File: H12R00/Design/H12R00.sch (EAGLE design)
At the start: 35 parts, among them P1 HEXABIT_17.32_NO_P3_P6, U1 STM32F091CBU6, U2 AD628ARZ, U3 REF193GSZ, X1 XTALL_CSTCE8M00G52

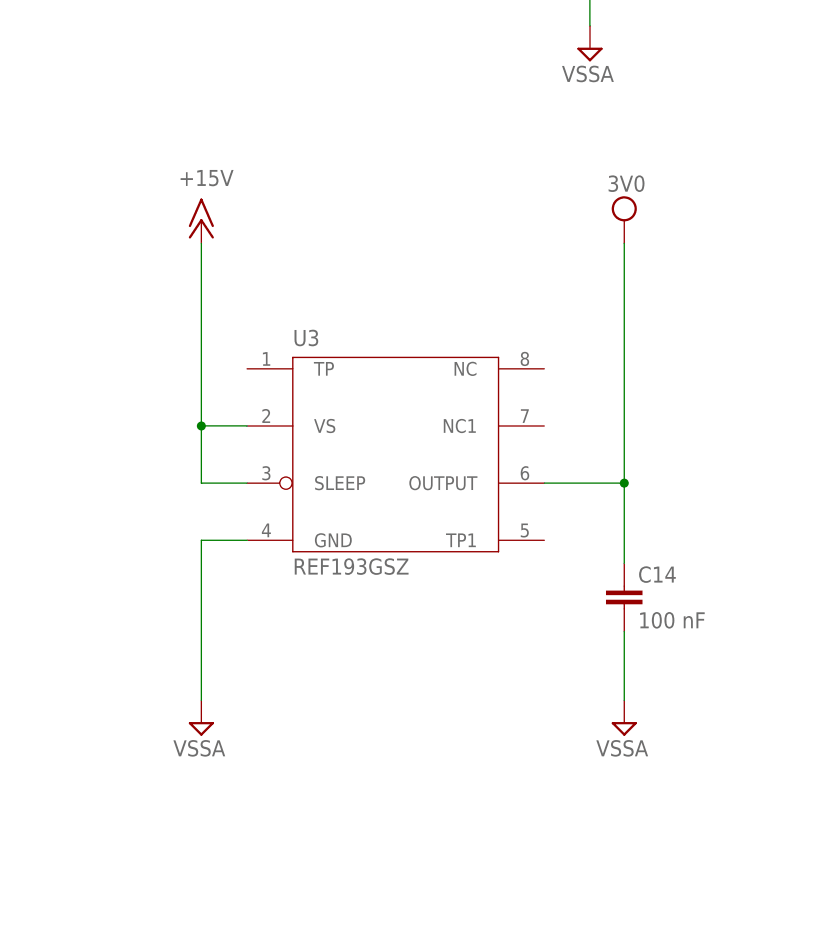
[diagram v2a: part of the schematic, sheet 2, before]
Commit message: Update REF from library Fix routing and DRC issues
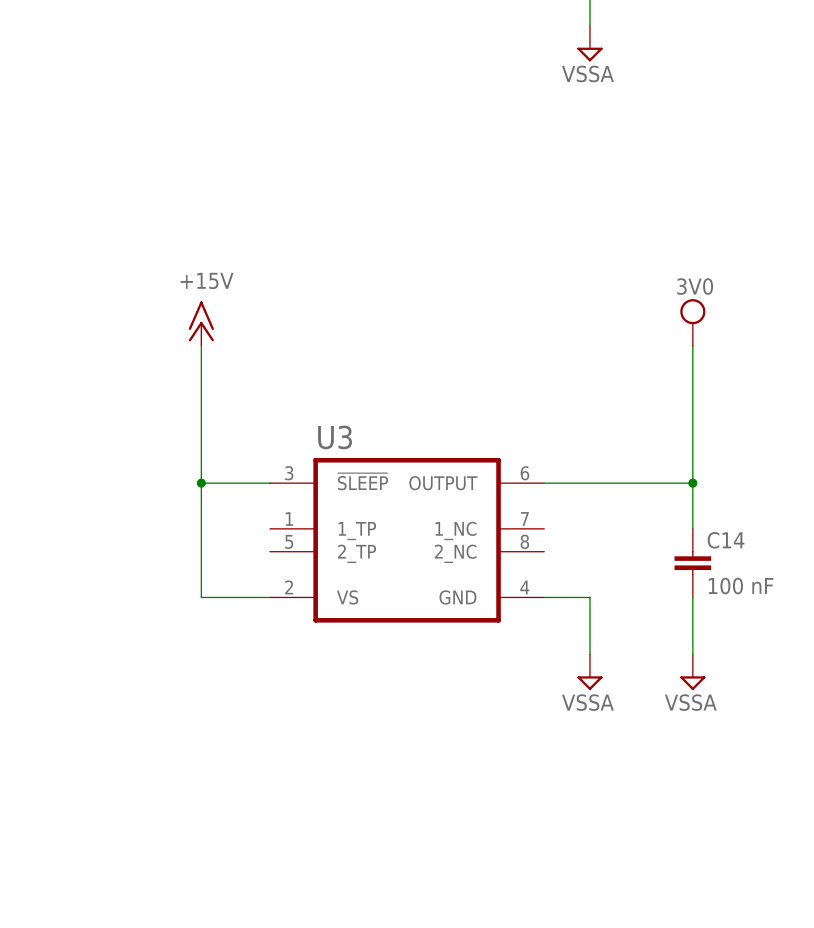
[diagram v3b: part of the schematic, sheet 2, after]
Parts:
- U3: device Hexabitz:REF193GSZ -> Hexabitz:REF193GSZANALOG_DEVICES_REF193GSZ_0_1
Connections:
- net +15V: now also U3.!SLEEP!; no longer U3.SLEEP
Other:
- moved on the sheet: C14
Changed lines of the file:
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@@
 <part name="SUPPLY16" library="supply2" deviceset="AGND" device="" value="VSSA"/>
 <part name="SUPPLY21" library="supply2" deviceset="AGND" device="" value="VSSA"/>
-<part name="U3" library="Hexabitz" deviceset="REF193GSZ" device=""/>
 <part name="C14" library="Hexabitz" deviceset="C-1206" device="" value="100 nF">
 <attribute name="CAPACITANCE" value="100 nF"/>
@@
 <part name="P+4" library="supply1" library_urn="urn:adsk.eagle:library:371" deviceset="+15V" device=""/>
 <part name="SUPPLY7" library="supply2" deviceset="VCC" device="" value="3V0"/>
+<part name="U3" library="Hexabitz" deviceset="REF193GSZ" device="ANALOG_DEVICES_REF193GSZ_0_1" value="REF193GSZ"/>
 </parts>
 <sheets>
@@
 <attribute name="VALUE" x="137.287" y="64.262" size="1.778" layer="96" rot="R180"/>
 </instance>
-<instance part="SUPPLY24" gate="G$1" x="234.95" y="66.04" smashed="yes">
-<attribute name="VALUE" x="237.617" y="64.135" size="1.778" layer="96" rot="R180"/>
+<instance part="SUPPLY24" gate="G$1" x="242.57" y="71.12" smashed="yes">
+<attribute name="VALUE" x="245.237" y="69.215" size="1.778" layer="96" rot="R180"/>
 </instance>
 <instance part="AIN" gate="-1" x="240.03" y="158.75" smashed="yes">
@@
 <attribute name="VALUE" x="77.597" y="73.025" size="1.778" layer="96" rot="R180"/>
 </instance>
-<instance part="U3" gate="G$1" x="209.55" y="95.25" smashed="yes">
-<attribute name="NAME" x="198.12" y="107.95" size="1.778" layer="95"/>
-<attribute name="VALUE" x="198.12" y="82.55" size="1.778" layer="96"/>
-</instance>
-<instance part="C14" gate="G$1" x="234.95" y="78.74" smashed="yes">
-<attribute name="NAME" x="236.474" y="81.661" size="1.778" layer="95"/>
-<attribute name="VALUE" x="236.474" y="76.581" size="1.778" layer="96"/>
-<attribute name="CAPACITANCE" x="234.95" y="78.74" size="1.778" layer="96" display="off"/>
-<attribute name="CAPACITANCE_TOLERANCE" x="234.95" y="78.74" size="1.778" layer="96" display="off"/>
-<attribute name="DESCREPTION" x="234.95" y="78.74" size="1.778" layer="96" display="off"/>
-<attribute name="MFN" x="234.95" y="78.74" size="1.778" layer="96" display="off"/>
-<attribute name="MPN" x="234.95" y="78.74" size="1.778" layer="96" display="off"/>
-<attribute name="OCTOPART_URL" x="234.95" y="78.74" size="1.778" layer="96" display="off"/>
-<attribute name="VOLTAGE_RATING" x="234.95" y="78.74" size="1.778" layer="96" display="off"/>
+<instance part="C14" gate="G$1" x="242.57" y="82.55" smashed="yes">
+<attribute name="NAME" x="244.094" y="85.471" size="1.778" layer="95"/>
+<attribute name="VALUE" x="244.094" y="80.391" size="1.778" layer="96"/>
+<attribute name="CAPACITANCE" x="242.57" y="82.55" size="1.778" layer="96" display="off"/>
+<attribute name="CAPACITANCE_TOLERANCE" x="242.57" y="82.55" size="1.778" layer="96" display="off"/>
+<attribute name="DESCREPTION" x="242.57" y="82.55" size="1.778" layer="96" display="off"/>
+<attribute name="MFN" x="242.57" y="82.55" size="1.778" layer="96" display="off"/>
+<attribute name="MPN" x="242.57" y="82.55" size="1.778" layer="96" display="off"/>
+<attribute name="OCTOPART_URL" x="242.57" y="82.55" size="1.778" layer="96" display="off"/>
+<attribute name="VOLTAGE_RATING" x="242.57" y="82.55" size="1.778" layer="96" display="off"/>
 </instance>
-<instance part="SUPPLY25" gate="G$1" x="187.96" y="66.04" smashed="yes">
-<attribute name="VALUE" x="190.627" y="64.135" size="1.778" layer="96" rot="R180"/>
+<instance part="SUPPLY25" gate="G$1" x="231.14" y="71.12" smashed="yes">
+<attribute name="VALUE" x="233.807" y="69.215" size="1.778" layer="96" rot="R180"/>
 </instance>
 <instance part="SUPPLY26" gate="G$1" x="231.14" y="140.97" smashed="yes">
@@
 <attribute name="VALUE" x="134.62" y="172.72" size="1.778" layer="96"/>
 </instance>
-<instance part="P+3" gate="1" x="187.96" y="121.92" smashed="yes">
-<attribute name="VALUE" x="185.42" y="125.73" size="1.778" layer="96"/>
+<instance part="P+3" gate="1" x="187.96" y="110.49" smashed="yes">
+<attribute name="VALUE" x="185.42" y="114.3" size="1.778" layer="96"/>
 </instance>
 <instance part="P+4" gate="1" x="74.93" y="114.3" smashed="yes">
 <attribute name="VALUE" x="72.39" y="118.11" size="1.778" layer="96"/>
 </instance>
-<instance part="SUPPLY7" gate="G$1" x="234.95" y="121.92" smashed="yes">
-<attribute name="VALUE" x="233.045" y="125.095" size="1.778" layer="96"/>
+<instance part="SUPPLY7" gate="G$1" x="242.57" y="110.49" smashed="yes">
+<attribute name="VALUE" x="240.665" y="113.665" size="1.778" layer="96"/>
+</instance>
+<instance part="U3" gate="G$0" x="210.82" y="87.63" smashed="yes">
+<attribute name="NAME" x="200.66" y="99.06" size="2.54" layer="95" align="top-left"/>
 </instance>
 </instances>
@@
 <pinref part="SUPPLY24" gate="G$1" pin="AGND"/>
 <pinref part="C14" gate="G$1" pin="2"/>
-<wire x1="234.95" y1="68.58" x2="234.95" y2="76.2" width="0.1524" layer="91"/>
-</segment>
-<segment>
-<pinref part="SUPPLY25" gate="G$1" pin="AGND"/>
-<wire x1="187.96" y1="68.58" x2="187.96" y2="86.36" width="0.1524" layer="91"/>
-<pinref part="U3" gate="G$1" pin="GND"/>
-<wire x1="187.96" y1="86.36" x2="193.04" y2="86.36" width="0.1524" layer="91"/>
+<wire x1="242.57" y1="73.66" x2="242.57" y2="80.01" width="0.1524" layer="91"/>
 </segment>
 <segment>
@@
 <junction x="86.36" y="147.32"/>
 </segment>
+<segment>
+<pinref part="U3" gate="G$0" pin="GND"/>
+<wire x1="226.06" y1="80.01" x2="231.14" y2="80.01" width="0.1524" layer="91"/>
+<wire x1="231.14" y1="80.01" x2="231.14" y2="73.66" width="0.1524" layer="91"/>
+<pinref part="SUPPLY25" gate="G$1" pin="AGND"/>
+</segment>
 </net>
 <net name="VIN" class="0">
@@
 </segment>
 <segment>
-<pinref part="U3" gate="G$1" pin="SLEEP"/>
-<wire x1="193.04" y1="92.71" x2="187.96" y2="92.71" width="0.1524" layer="91"/>
-<wire x1="187.96" y1="92.71" x2="187.96" y2="99.06" width="0.1524" layer="91"/>
-<pinref part="U3" gate="G$1" pin="VS"/>
-<wire x1="187.96" y1="99.06" x2="187.96" y2="119.38" width="0.1524" layer="91"/>
-<wire x1="193.04" y1="99.06" x2="187.96" y2="99.06" width="0.1524" layer="91"/>
-<junction x="187.96" y="99.06"/>
+<wire x1="195.58" y1="92.71" x2="187.96" y2="92.71" width="0.1524" layer="91"/>
+<wire x1="187.96" y1="92.71" x2="187.96" y2="107.95" width="0.1524" layer="91"/>
 <pinref part="P+3" gate="1" pin="+15V"/>
+<pinref part="U3" gate="G$0" pin="!SLEEP!"/>
+<pinref part="U3" gate="G$0" pin="VS"/>
+<wire x1="195.58" y1="80.01" x2="187.96" y2="80.01" width="0.1524" layer="91"/>
+<wire x1="187.96" y1="80.01" x2="187.96" y2="92.71" width="0.1524" layer="91"/>
+<junction x="187.96" y="92.71"/>
 </segment>
 <segment>
@@
 <pinref part="SUPPLY7" gate="G$1" pin="VCC"/>
 <pinref part="C14" gate="G$1" pin="1"/>
-<wire x1="234.95" y1="83.82" x2="234.95" y2="92.71" width="0.1524" layer="91"/>
-<pinref part="U3" gate="G$1" pin="OUTPUT"/>
-<wire x1="234.95" y1="92.71" x2="226.06" y2="92.71" width="0.1524" layer="91"/>
-<wire x1="234.95" y1="119.38" x2="234.95" y2="92.71" width="0.1524" layer="91"/>
-<junction x="234.95" y="92.71"/>
+<wire x1="242.57" y1="87.63" x2="242.57" y2="92.71" width="0.1524" layer="91"/>
+<wire x1="242.57" y1="92.71" x2="226.06" y2="92.71" width="0.1524" layer="91"/>
+<wire x1="242.57" y1="107.95" x2="242.57" y2="92.71" width="0.1524" layer="91"/>
+<junction x="242.57" y="92.71"/>
+<pinref part="U3" gate="G$0" pin="OUTPUT"/>
 </segment>
 </net>
